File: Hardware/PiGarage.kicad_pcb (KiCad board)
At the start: 2 copper layers, 65 x 56 mm, 75 parts, among them J1 Conn_02x03_Odd_Even, J2 Conn_02x02_Counter_Clockwise, J3 PJ-320B, J4 Conn_02x20_Odd_Even, Q1 MMBT3904, U1 PCM5122PWR, U2 TPS54560BQDDARQ1, U3 TL431DBZ, U4 AP2112K-3.3, U5 Optocoupler_DC_PhotoNPN_AKEC, U6 Optocoupler_DC_PhotoNPN_AKEC, U7 Optocoupler_DC_PhotoNPN_AKEC, U8 Optocoupler_DC_PhotoNPN_AKEC, U9 ADS1115IDGS

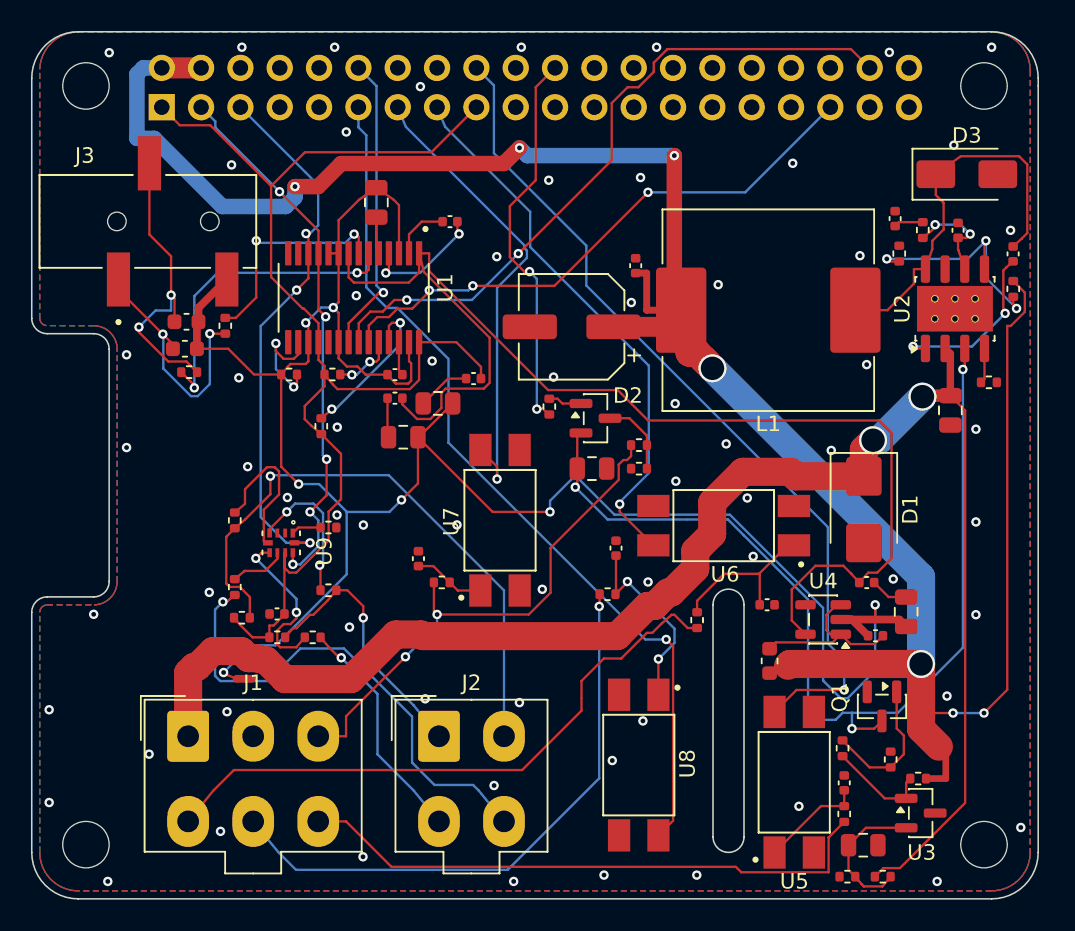
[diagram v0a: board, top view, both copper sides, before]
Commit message: v0.2
- Buck converter redesigned with TI WEBENCH (7-16V in, 5V/5A, 1.1MHz fsw)
- New inductor: FXL0630-2R2-M (2.2µH, 10A Isat, 15mΩ DCR)
- New catch diode: B560C-13-F (SMC package for better thermals)
- Added AO4407A P-FET reverse polarity protection
- Replaced 4× LTV-817S with 1× LTV-847S quad optocoupler
- Switched ADS1115 back to VSSOP (IDGSR) from QFN
- All passives upgraded from 0402 to 0603 for hand-solder friendliness
- Fixed DAC pin connections (BCM21 for DIN, XSMT to 3.3VA)
- Fixed ADC pull-up topology for correct voltage divider operation
- Merged AGND into GND (shared ground per PCM5122 datasheet)
- Added GND via stitching (65 vias)
- Updated all 3D model paths for KiCad 10
- Updated BOM, design notes, and README
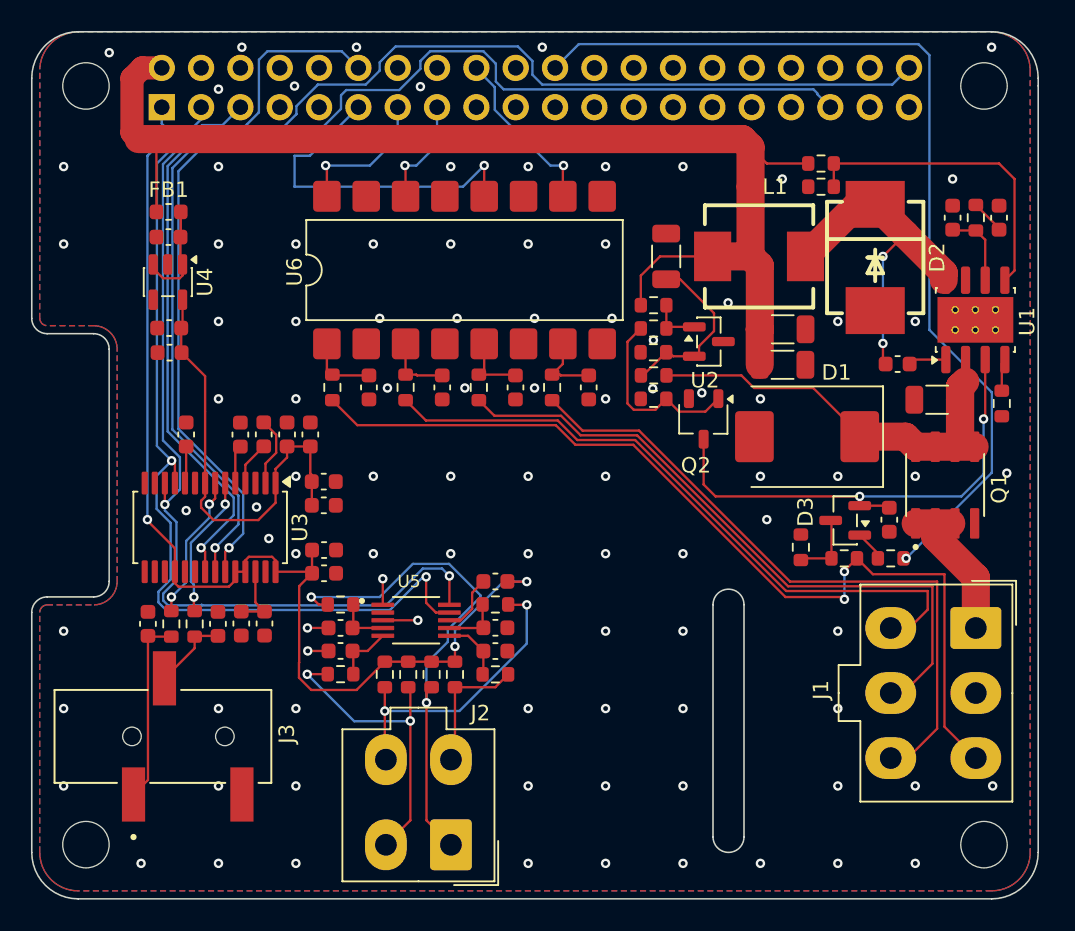
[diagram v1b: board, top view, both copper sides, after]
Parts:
- removed NT1: NetTie_2, NetTie:NetTie-2_SMD_Pad0.5mm
- removed R27, R28: 4.7kΩ, Resistor_SMD:R_0402_1005Metric
- removed U7, U8: Optocoupler_DC_PhotoNPN_AKEC, FOD817BSD:SOIC254P1016X385-4N
- removed U9: ADS1115IDGS, ADS1115IRUGR:IC_ADS1115IRUGR
- added C26: 100nF, Capacitor_SMD:C_0603_1608Metric, F.Cu at (99.0, 56.0)
- added C27: 100nF, Capacitor_SMD:C_0603_1608Metric, F.Cu at (103.8, 56.0)
- added C28: 100nF, Capacitor_SMD:C_0603_1608Metric, F.Cu at (108.5, 56.0)
- added C29: 100nF, Capacitor_SMD:C_0603_1608Metric, F.Cu at (92.5, 71.5)
- added C30: 100nF, Capacitor_SMD:C_0603_1608Metric, F.Cu at (92.5, 73.0)
- added C31: 100nF, Capacitor_SMD:C_0603_1608Metric, F.Cu at (102.5, 73.0)
- added C32: 100nF, Capacitor_SMD:C_0603_1608Metric, F.Cu at (102.5, 71.5)
- added C33: 100nF, Capacitor_SMD:C_0603_1608Metric, F.Cu at (102.5, 68.5)
- added Q2: MMBT3904, Package_TO_SOT_SMD:TSOT-23, F.Cu at (115.9, 58.0)
- C1: value 10µF -> 4.7µF; footprint Capacitor_SMD:C_0805_2012Metric -> Capacitor_SMD:C_1206_3216Metric
- C10: value 10µF -> 100nF; footprint Capacitor_SMD:C_0805_2012Metric -> Capacitor_SMD:C_0603_1608Metric
- C11, C20, C22: value 100nF -> 10µF; footprint Capacitor_SMD:C_0402_1005Metric -> Capacitor_SMD:C_0603_1608Metric
- C12, C16: footprint Capacitor_SMD:C_0805_2012Metric -> Capacitor_SMD:C_0603_1608Metric
- C13, C21: value 100nF -> 0.1µF; footprint Capacitor_SMD:C_0402_1005Metric -> Capacitor_SMD:C_0603_1608Metric
- C14: value 10µF -> 2.2µF; footprint Capacitor_SMD:C_0805_2012Metric -> Capacitor_SMD:C_0603_1608Metric
- C15: value 100nF -> 2.2µF; footprint Capacitor_SMD:C_0402_1005Metric -> Capacitor_SMD:C_0603_1608Metric
- C17: value 1µF -> 0.1µF; footprint Capacitor_SMD:C_0402_1005Metric -> Capacitor_SMD:C_0603_1608Metric
- C18: value 2.2nF -> 10µF
- C19: value 2.2nF -> 0.1µF
- C2, C25: footprint Capacitor_SMD:C_0402_1005Metric -> Capacitor_SMD:C_0603_1608Metric
- C23: value 100nF -> 2.2nF; footprint Capacitor_SMD:C_0402_1005Metric -> Capacitor_SMD:C_0603_1608Metric
- C24: value 1µF -> 2.2nF; footprint Capacitor_SMD:C_0402_1005Metric -> Capacitor_SMD:C_0603_1608Metric
- C3: value 1µF -> 1.8nF; footprint Capacitor_SMD:C_0402_1005Metric -> Capacitor_SMD:C_0603_1608Metric
- C4: value 47µF -> 8.2pF; footprint Capacitor_SMD:CP_Elec_6.3x5.7 -> Capacitor_SMD:C_0603_1608Metric
- C5: value 47pF -> 47µF; footprint Capacitor_SMD:C_0402_1005Metric -> Capacitor_SMD:C_1206_3216Metric
- C6: value 1nF -> 47µF; footprint Capacitor_SMD:C_0402_1005Metric -> Capacitor_SMD:C_1206_3216Metric
- C7: value 10µF -> 47µF; footprint Capacitor_SMD:C_0805_2012Metric -> Capacitor_SMD:C_1206_3216Metric
- C8: value 47µF -> 10µF; footprint Capacitor_SMD:C_0805_2012Metric -> Capacitor_SMD:C_0603_1608Metric
- C9: value 100nF -> 1µF; footprint Capacitor_SMD:C_0402_1005Metric -> Capacitor_SMD:C_0603_1608Metric
- D1: value D_TVS -> SMBJ18CA; footprint Diode_SMD:D_SMB -> Diode_SMD:D_SMC
- D2: value D_Schottky_Dual_CommonCathode_AKA -> B560C-13-F; footprint Package_TO_SOT_SMD:SOT-23 -> B560C:SMC_L7.1-W6.2-LS8.1-RD
- D3: value D_Schottky -> BAT54CLT1G; footprint Diode_SMD:D_SMA -> Package_TO_SOT_SMD:SOT-23
- L1: value 10µH -> 2.2µH; footprint Inductor_SMD:L_Sunlord_MWSA1204S-100 -> FXL0630:IND-SMD_L7.0-W6.6
- Q1: value MMBT3904 -> AO4407A; footprint Package_TO_SOT_SMD:SOT-23 -> SOIC127P600X175:SOIC127P600X175-8N
- R1: value 200kΩ -> 23.7kΩ; footprint Resistor_SMD:R_0402_1005Metric -> Resistor_SMD:R_0603_1608Metric
- R10: value 22kΩ -> 100kΩ; footprint Resistor_SMD:R_0402_1005Metric -> Resistor_SMD:R_0603_1608Metric
- R11: value 1kΩ -> 4.7kΩ; footprint Resistor_SMD:R_0402_1005Metric -> Resistor_SMD:R_0603_1608Metric
- R12: value 47kΩ -> 22kΩ; footprint Resistor_SMD:R_0402_1005Metric -> Resistor_SMD:R_0603_1608Metric
- R13, R14: value 10kΩ -> 470Ω; footprint Resistor_SMD:R_0402_1005Metric -> Resistor_SMD:R_0603_1608Metric
- R15, R16: value 470Ω -> 10kΩ; footprint Resistor_SMD:R_0402_1005Metric -> Resistor_SMD:R_0603_1608Metric
- R17, R18, R21, R23, R24, R25, R26, R6: footprint Resistor_SMD:R_0402_1005Metric -> Resistor_SMD:R_0603_1608Metric
- R19, R20, R22: value 10kΩ -> 4.7kΩ; footprint Resistor_SMD:R_0402_1005Metric -> Resistor_SMD:R_0603_1608Metric
- R2: value 52.3kΩ -> 80.6kΩ; footprint Resistor_SMD:R_0402_1005Metric -> Resistor_SMD:R_0603_1608Metric
- R3: value 10kΩ -> 60.4kΩ; footprint Resistor_SMD:R_0402_1005Metric -> Resistor_SMD:R_0603_1608Metric
- R4: value 15kΩ -> 11.5kΩ; footprint Resistor_SMD:R_0402_1005Metric -> Resistor_SMD:R_0603_1608Metric
- R5: value 10kΩ -> 84.5kΩ; footprint Resistor_SMD:R_0402_1005Metric -> Resistor_SMD:R_0603_1608Metric
- R7: value 10kΩ -> 1kΩ; footprint Resistor_SMD:R_0402_1005Metric -> Resistor_SMD:R_0603_1608Metric
- R8: value 100kΩ -> 47kΩ; footprint Resistor_SMD:R_0402_1005Metric -> Resistor_SMD:R_0603_1608Metric
- R9: value 84.5kΩ -> 10kΩ; footprint Resistor_SMD:R_0402_1005Metric -> Resistor_SMD:R_0603_1608Metric
- U1: value PCM5122PWR -> TPS54560BQDDARQ1; footprint PCM5122PWR:SOP65P640X120-28N -> Package_SO:Texas_R-PDSO-G8_EP2.95x4.9mm_Mask2.4x3.1mm_ThermalVias
- U2: value TPS54560BQDDARQ1 -> TL431DBZ; footprint Package_SO:Texas_R-PDSO-G8_EP2.95x4.9mm_Mask2.4x3.1mm_ThermalVias -> Package_TO_SOT_SMD:SOT-23
- U3: value TL431DBZ -> PCM5122PWR; footprint Package_TO_SOT_SMD:SOT-23 -> Package_SO:TSSOP-28_4.4x9.7mm_P0.65mm
- U5: value Optocoupler_DC_PhotoNPN_AKEC -> ADS1115IDGSR; footprint FOD817BSD:SOIC254P1016X385-4N -> ADS1115IDGSR:SOP50P490X110-10N
- U6: value Optocoupler_DC_PhotoNPN_AKEC -> LTV-847S; footprint FOD817BSD:SOIC254P1016X385-4N -> Package_DIP:SMDIP-16_W9.53mm
- moved J1 51.4 mm to (133.5, 71.5), turned to -90 degrees
- moved C10 50.4 mm to (81.4, 53.7), turned to 0 degrees
- moved C9 50.3 mm to (81.4, 46.3)
- moved U3 49.5 mm to (84.0, 65.0), turned to -90 degrees
- moved REF** 48.7 mm to (79.0, 78.9), turned to 180 degrees
- moved FB1 48.4 mm to (81.4, 44.6), turned to 0 degrees
- moved U4 47.6 mm to (81.3, 49.2), turned to -90 degrees
- moved C24 47.0 mm to (80.0, 71.2), turned to 90 degrees
- moved R13 45.8 mm to (83.0, 71.2)
- moved U1 40.2 mm to (133.5, 51.6), turned to 90 degrees
- moved C25 39.9 mm to (94.3, 56.0), turned to -90 degrees
- moved C15 34.3 mm to (87.5, 59.0), turned to -90 degrees
- moved R9 34.2 mm to (112.7, 56.7)
- moved J3 33.3 mm to (82.0, 78.5)
- moved R7 30.4 mm to (112.7, 50.7), turned to 180 degrees
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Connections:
- C1 pad 1: +VBAT -> Net-(D1-A1)
- C10 pad 1: AGND -> GND
- C10 pad 2: Net-(C10-Pad2) -> +3.3VA
- C11 pad 1: +3.3V -> GND
- C11 pad 2: Net-(C11-Pad2) -> +3.3VA
- C12 pad 1: Net-(C11-Pad2) -> GND
- C12 pad 2: AGND -> Net-(U3-LDOO)
- C13 pad 1: +3.3VA -> GND
- C13 pad 2: Net-(C13-Pad2) -> Net-(U3-LDOO)
- C14 pad 1: Net-(C13-Pad2) -> Net-(U3-VNEG)
- C14 pad 2: AGND -> GND
- C15 pad 1: Net-(C15-Pad1) -> Net-(U3-CAPP)
- C15 pad 2: GND -> Net-(U3-CAPM)
- C16 pad 1: Net-(U1-VNEG) -> GND
- C16 pad 2: AGND -> Net-(U3-VCOM)
- C17 pad 1: Net-(U1-CAPP) -> +3.3V
- C17 pad 2: Net-(U1-CAPM) -> GND
- C18 pad 1: AGND -> GND
- C18 pad 2: Net-(C18-Pad2) -> +3.3V
- C19 pad 1: Net-(C19-Pad1) -> +3.3VA
- C19 pad 2: AGND -> GND
- C2 pad 1: Net-(U2-BOOT) -> Net-(U1-BOOT)
- C2 pad 2: Net-(D3-K) -> Net-(D2-K)
- C20 pad 1: AGND -> GND
- C20 pad 2: Net-(U1-LDOO) -> +3.3VA
- C21 pad 1: Net-(C21-Pad1) -> +3.3VA
- C22 pad 1: Net-(C22-Pad1) -> GND
- C22 pad 2: GND -> +3.3VA
- C23 pad 1: +3.3V -> GND
- C23 pad 2: GND -> Net-(C23-Pad2)
- C24 pad 1: +5VA -> Net-(C24-Pad1)
- C24 pad 2: AGND -> GND
- C3 pad 1: +5V -> Net-(C3-Pad1)
- C4 pad 1: +5V -> Net-(U1-COMP)
- C5 pad 1: Net-(U2-COMP) -> +5V
- C6 pad 1: Net-(C6-Pad1) -> +5V
- C7 pad 1: /EN -> GND
- C7 pad 2: GND -> Net-(U2-REF)
- C8 pad 1: GND -> /EN
- C8 pad 2: Net-(U3-REF) -> GND
- C9 pad 1: Net-(C10-Pad2) -> +5VA
- C9 pad 2: +3.3VA -> GND
- D1 pad 1: +VBAT -> Net-(D1-A1)
- D2 pad 1: Net-(D2-A-Pad1) -> Net-(D2-K)
- D2 pad 2: /EN -> GND
- D3 pad 1: Net-(D3-K) -> Net-(D3-A-Pad1)
- D3 pad 2: GND -> /EN
- J3 pad 1: Net-(C19-Pad1) -> Net-(C24-Pad1)
- J3 pad 2: Net-(C18-Pad2) -> Net-(C23-Pad2)
- J3 pad 3: AGND -> GND
- J4 pad 38: /BCM20 -> unconnected-(J4-Pin_38-Pad38)
- J4 pad 40: unconnected-(J4-Pin_40-Pad40) -> /BCM21
- L1 pad 1: Net-(D3-K) -> Net-(D2-K)
- Q1 pad 1: Net-(Q1-B) -> +VBAT
- Q1 pad 2: GND -> +VBAT
- Q1 pad 3: /EN -> +VBAT
- R1 pad 1: Net-(U2-RT/CLK) -> Net-(C3-Pad1)
- R1 pad 2: GND -> Net-(U1-COMP)
- R10 pad 1: GND -> /ACC
- R10 pad 2: Net-(U3-REF) -> Net-(D3-A-Pad3)
- R11 pad 1: Net-(U3-K) -> /BCM25
- R11 pad 2: +5V -> Net-(D3-A-Pad1)
- R12 pad 1: Net-(U3-K) -> GND
- R12 pad 2: Net-(Q1-B) -> Net-(D3-A-Pad3)
- R13 pad 1: Net-(Q1-B) -> Net-(C23-Pad2)
- R13 pad 2: GND -> /OUTL
- R14 pad 1: +3.3V -> /OUTR
- R14 pad 2: Net-(U1-XSMT) -> Net-(C24-Pad1)
- R15 pad 1: Net-(C18-Pad2) -> /ACC
- R15 pad 2: /OUTL -> Net-(C25-Pad1)
- R16 pad 1: /OUTR -> /ILL
- R16 pad 2: Net-(C19-Pad1) -> Net-(C26-Pad1)
- R17 pad 1: +3.3V -> /REV
- R17 pad 2: Net-(U1-ADR1) -> Net-(C27-Pad1)
- R18 pad 1: AGND -> /AUX
- R18 pad 2: Net-(U1-ADR2) -> Net-(C28-Pad1)
- R19 pad 1: /AUX -> /AIN0
- R19 pad 2: Net-(C25-Pad1) -> +3.3V
- R2 pad 1: Net-(U2-FB) -> Net-(U1-RT/CLK)
- R2 pad 2: +5V -> GND
- R20 pad 1: /ILL -> /AIN1
- R20 pad 2: Net-(C15-Pad1) -> +3.3V
- R21 pad 1: /BCM25 -> /AIN2
- R21 pad 2: Net-(D2-A-Pad1) -> +3.3V
- R22 pad 1: /ACC -> /AIN3
- R22 pad 2: Net-(C21-Pad1) -> +3.3V
- R23 pad 1: /AIN2 -> Net-(U5-AIN0)
- R23 pad 2: Net-(U9-AIN2) -> /AIN0
- R24 pad 1: /REV -> Net-(U5-AIN1)
- R24 pad 2: Net-(C22-Pad1) -> /AIN1
- R25 pad 1: /AIN3 -> Net-(U5-AIN2)
- R25 pad 2: Net-(U9-AIN3) -> /AIN2
- R26 pad 1: Net-(U9-ADDR) -> Net-(U5-AIN3)
- R26 pad 2: GND -> /AIN3
- R3 pad 1: Net-(U2-FB) -> Net-(U1-FB)
- R3 pad 2: GND -> +5V
- R4 pad 1: Net-(U2-COMP) -> Net-(U1-FB)
- R4 pad 2: Net-(C6-Pad1) -> GND
- R5 pad 1: /AIN0 -> Net-(U2-REF)
- R5 pad 2: Net-(U9-AIN0) -> Net-(D1-A1)
- R6 pad 2: Net-(D2-A-Pad3) -> Net-(U2-REF)
- R7 pad 1: /AIN1 -> Net-(U2-K)
- R7 pad 2: Net-(U9-AIN1) -> +5V
- R8 pad 1: /ACC -> Net-(U2-K)
- R8 pad 2: Net-(D2-A-Pad3) -> Net-(Q2-B)
- R9 pad 1: Net-(U3-REF) -> Net-(Q2-B)
- R9 pad 2: +VBAT -> GND
- U1 pad 1: +3.3VA -> Net-(U1-BOOT)
- U1 pad 2: Net-(U1-CAPP) -> Net-(D1-A1)
- U1 pad 3: AGND -> /EN
- U1 pad 4: Net-(U1-CAPM) -> Net-(U1-RT/CLK)
- U1 pad 5: Net-(U1-VNEG) -> Net-(U1-FB)
- U1 pad 6: /OUTL -> Net-(U1-COMP)
- U1 pad 7: /OUTR -> GND
- U1 pad 8: +3.3VA -> Net-(D2-K)
- U1 pad 9: AGND -> GND
- U2 pad 1: Net-(U2-BOOT) -> Net-(U2-K)
- U2 pad 2: +VBAT -> Net-(U2-REF)
- U2 pad 3: /EN -> GND
- U3 pad 1: Net-(U3-K) -> +3.3VA
- U3 pad 2: Net-(U3-REF) -> Net-(U3-CAPP)
- U3 pad 3: GND -> unconnected-(U3-CPGND-Pad3)
- U4 pad 2: AGND -> GND
- U5 pad 1: Net-(C25-Pad1) -> GND
- U5 pad 2: GND -> unconnected-(U5-ALERT/RDY-Pad2)
- U5 pad 4: /BCM24 -> Net-(U5-AIN0)
- U6 pad 1: Net-(C15-Pad1) -> Net-(C25-Pad1)
- U6 pad 3: GND -> Net-(C26-Pad1)
- U6 pad 4: /BCM22 -> GND
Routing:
- net AGND: track 136.8 -> 0.00 mm, vias 7 -> 0
- net +VBAT: track 103.1 -> 10.1 mm, vias 2 -> 0
- net /BCM21: track 0.00 -> 81.9 mm, vias 0 -> 1
- net +5V: track 148.4 -> 78.9 mm, vias 7 -> 0
- net +3.3VA: track 81.4 -> 28.9 mm
- net /BCM20: track 44.6 -> 0.00 mm, vias 2 -> 0
- net /BCM24: track 55.1 -> 11.1 mm
- net /BCM19: track 36.8 -> 76.4 mm, vias 3 -> 1
- net /BCM25: track 25.1 -> 61.6 mm, vias 2 -> 1
- net /BCM17: track 57.1 -> 22.2 mm
- net /EN: track 63.3 -> 31.5 mm, vias 3 -> 2
- net Net-(D1-A1): track 0.00 -> 29.2 mm
- net /BCM22: track 35.5 -> 7.06 mm
- net /BCM18: track 19.5 -> 46.8 mm
- net /ACC: track 34.0 -> 60.2 mm
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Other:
- board text added: "v0.2"
- board text removed: "v0.1"

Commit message: Add thermal pad to D2 and remap GPIO sense pins
- Added exposed copper thermal pad (GND, pad 3) with 4 thermal vias to
  D2 (B560C catch diode) footprint for improved heat dissipation at 5A
- Remapped optoisolator GPIO assignments for cleaner PCB trace routing:
    BCM17 = ACC, BCM22 = REV, BCM27 = ILL, BCM24 = AUX
- Updated power_latch.py PIN_ACC 27 → 17 to match new assignment
- Updated design-notes and GPIO allocation table
- Cleaned up stale SVG exports from Images/
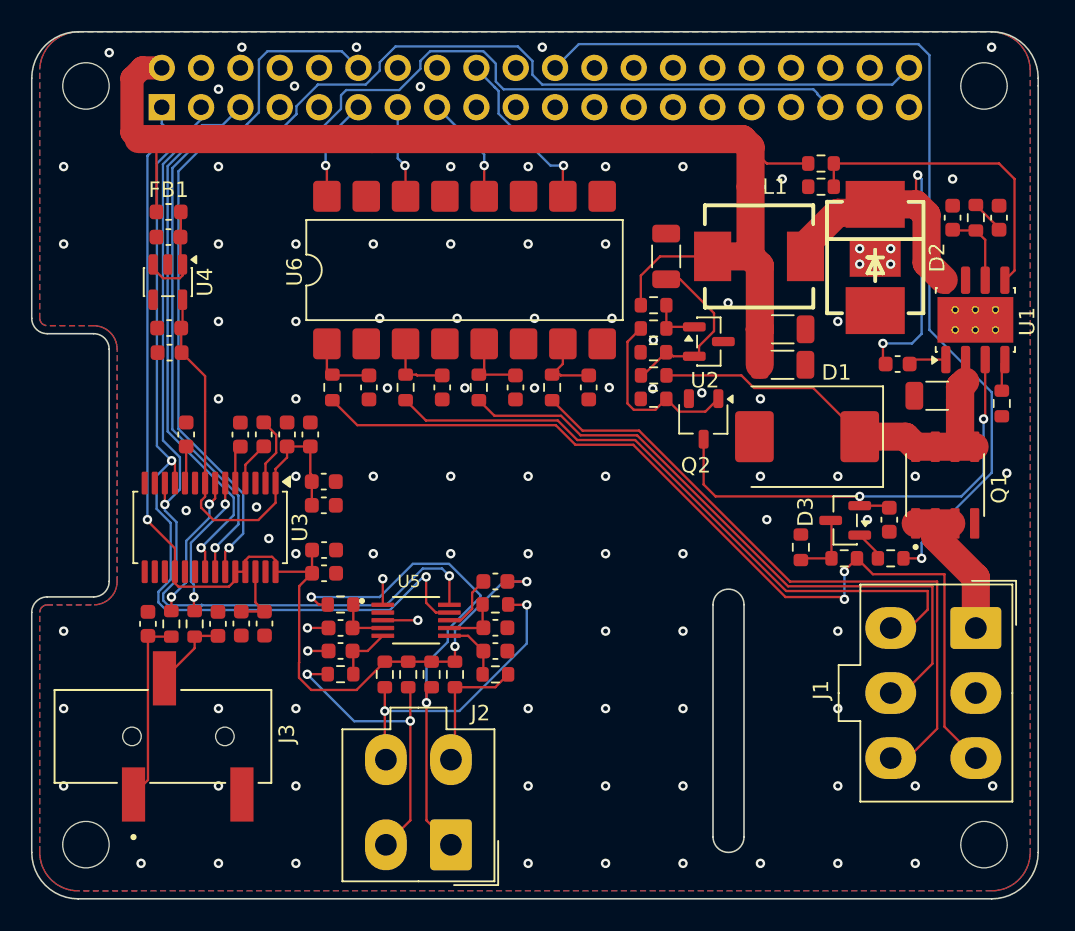
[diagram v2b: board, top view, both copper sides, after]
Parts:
- moved C1 0.26 mm to (131.0, 56.5)
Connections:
- U6 pad 12: /BCM17 -> /BCM22
- U6 pad 14: /BCM22 -> /BCM27
- U6 pad 16: /BCM27 -> /BCM17
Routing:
- net /BCM17: track 22.2 -> 6.66 mm
- net Net-(D2-K): track 21.6 -> 31.0 mm
- net /BCM27: track 9.39 -> 5.96 mm
- net /BCM25: track 61.6 -> 62.3 mm
- net GND: vias 94 -> 98

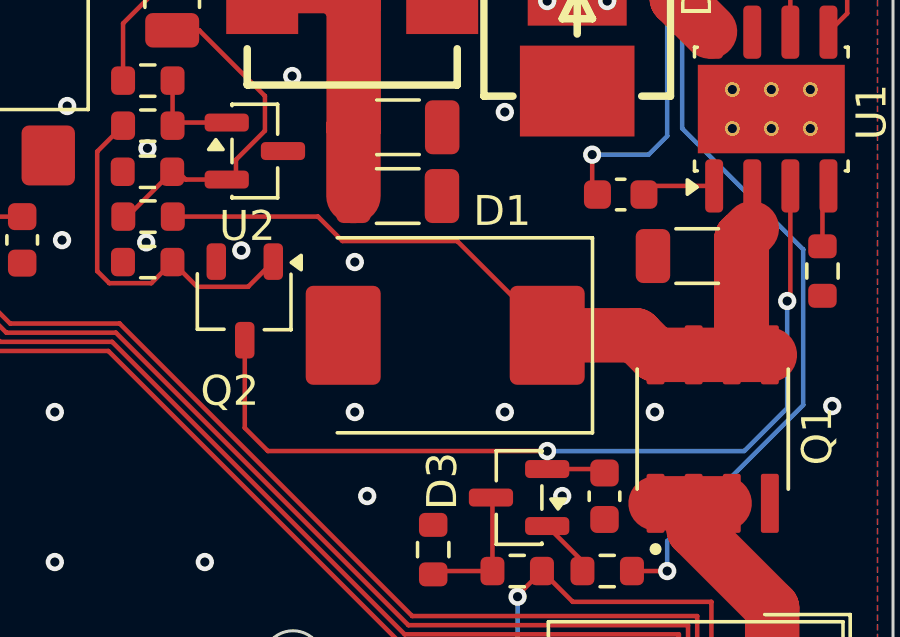
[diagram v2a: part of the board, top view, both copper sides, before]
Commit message: Fix D1 footprint: D_SMC (DO-214AB) → D_SMB (DO-214AA)
SMBJ18CA ships in SMB (DO-214AA) package; the SMC footprint had
~60% larger pads and courtyard, causing JLCPCB preview mismatch.
Updated pad positions (±3.4 → ±2.15 mm), pad size (3.3×2.5 →
2.5×2.3 mm), courtyard, silkscreen, fab outline, and 3D model to
match KiCad Diode_SMD:D_SMB. Re-routing of D1 connections required
in KiCad after this change.
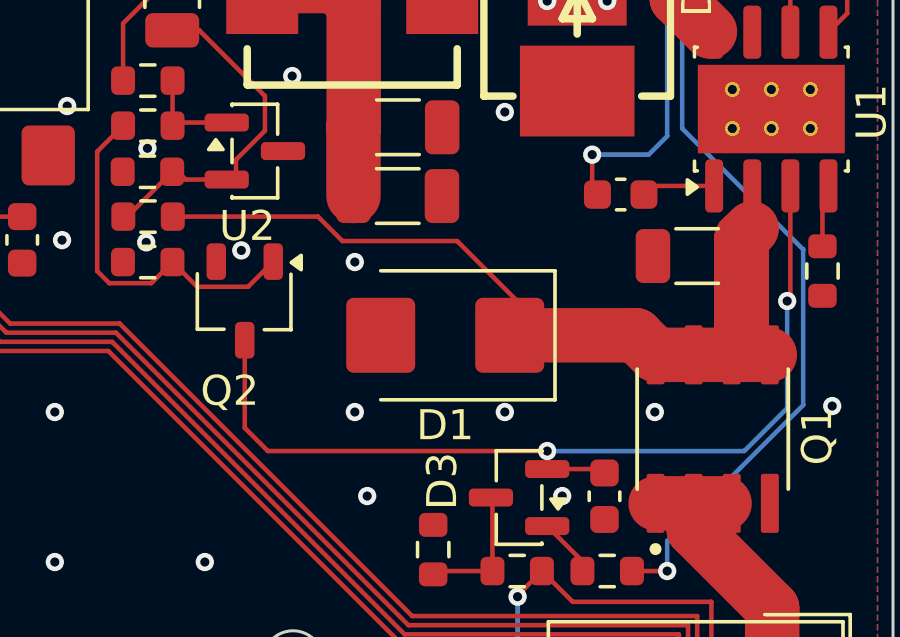
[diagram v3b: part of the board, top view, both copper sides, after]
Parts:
- D1: footprint Diode_SMD:D_SMC -> Diode_SMD:D_SMB
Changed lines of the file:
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@@
 		(filling no)
 		(pcbplotparams
-			(layerselection 0x00000000_00000000_55555555_55555551)
-			(plot_on_all_layers_selection 0x00000000_00000000_00000008_02000000)
+			(layerselection 0x00000000_00000000_55555555_55555554)
+			(plot_on_all_layers_selection 0x00000000_00000000_00000000_02000000)
 			(disableapertmacros no)
 			(usegerberextensions no)
@@
 			(plot_black_and_white no)
 			(sketchpadsonfab yes)
-			(plotpadnumbers yes)
+			(plotpadnumbers no)
 			(hidednponfab no)
 			(sketchdnponfab yes)
@@
 		)
 	)
-	(footprint "Diode_SMD:D_SMC"
+	(footprint "Diode_SMD:D_SMB"
 		(layer "F.Cu")
 		(at 122.6 59.141679 180)
-		(descr "Diode SMC (DO-214AB)")
-		(tags "Diode SMC (DO-214AB)")
+		(descr "Diode SMB (DO-214AA)")
+		(tags "Diode SMB (DO-214AA)")
 		(property "Reference" "D1"
-			(at -1.9 4.141679 0)
+			(at 0 -3 0)
 			(layer "F.SilkS")
 			(effects
@@
 		)
 		(property "Value" "SMBJ18CA"
-			(at 0 4.2 0)
+			(at 0 3.1 0)
 			(layer "F.Fab")
 			(effects
@@
 		(duplicate_pad_numbers_are_jumpers no)
 		(fp_line
-			(start -4.91 3.25)
-			(end 3.6 3.25)
+			(start -3.66 2.15)
+			(end 2.15 2.15)
 			(stroke
 				(width 0.12)
@@
 		)
 		(fp_line
-			(start -4.91 3.25)
-			(end -4.91 -3.25)
+			(start -3.66 -2.15)
+			(end -3.66 2.15)
 			(stroke
 				(width 0.12)
@@
 		)
 		(fp_line
-			(start -4.91 -3.25)
-			(end 3.6 -3.25)
+			(start -3.66 -2.15)
+			(end 2.15 -2.15)
 			(stroke
 				(width 0.12)
@@
 		)
 		(fp_line
-			(start 4.9 3.35)
-			(end -4.9 3.35)
+			(start 3.65 2.25)
+			(end -3.65 2.25)
 			(stroke
 				(width 0.05)
@@
 		)
 		(fp_line
-			(start 4.9 -3.35)
-			(end 4.9 3.35)
+			(start 3.65 -2.25)
+			(end 3.65 2.25)
 			(stroke
 				(width 0.05)
@@
 		)
 		(fp_line
-			(start -4.9 3.35)
-			(end -4.9 -3.35)
+			(start -3.65 2.25)
+			(end -3.65 -2.25)
 			(stroke
 				(width 0.05)
@@
 		)
 		(fp_line
-			(start -4.9 -3.35)
-			(end 4.9 -3.35)
+			(start -3.65 -2.25)
+			(end 3.65 -2.25)
 			(stroke
 				(width 0.05)
@@
 		)
 		(fp_line
-			(start 3.55 3.1)
-			(end -3.55 3.1)
+			(start 2.3 2)
+			(end -2.3 2)
 			(stroke
 				(width 0.1)
@@
 		)
 		(fp_line
-			(start 3.55 -3.1)
-			(end 3.55 3.1)
+			(start 2.3 -2)
+			(end 2.3 2)
 			(stroke
 				(width 0.1)
@@
 		)
 		(fp_line
-			(start 3.55 -3.1)
-			(end -3.55 -3.1)
+			(start 2.3 -2)
+			(end -2.3 -2)
 			(stroke
 				(width 0.1)
@@
 		)
 		(fp_line
-			(start -3.55 3.1)
-			(end -3.55 -3.1)
+			(start -2.3 2)
+			(end -2.3 -2)
 			(stroke
 				(width 0.1)
@@
 		)
 		(fp_text user "${REFERENCE}"
-			(at 0 -1.9 0)
+			(at 0 -3 0)
 			(layer "F.Fab")
 			(effects
@@
 		)
 		(pad "1" smd roundrect
-			(at -3.4 0 270)
-			(size 3.3 2.5)
+			(at -2.15 0 270)
+			(size 2.5 2.3)
 			(layers "F.Cu" "F.Mask" "F.Paste")
-			(roundrect_rratio 0.1)
+			(roundrect_rratio 0.1086956522)
 			(net "Net-(D1-A1)")
 			(pinfunction "A1_1")
@@
 		)
 		(pad "2" smd roundrect
-			(at 3.4 0 270)
-			(size 3.3 2.5)
+			(at 2.15 0 270)
+			(size 2.5 2.3)
 			(layers "F.Cu" "F.Mask" "F.Paste")
-			(roundrect_rratio 0.1)
+			(roundrect_rratio 0.1086956522)
 			(net "GND")
 			(pinfunction "A2_2")
@@
 		)
 		(embedded_fonts no)
-		(model "${KICAD10_3DMODEL_DIR}/Diode_SMD.3dshapes/D_SMC.step"
+		(model "${KICAD10_3DMODEL_DIR}/Diode_SMD.3dshapes/D_SMB.step"
 			(offset
 				(xyz 0 0 0)
